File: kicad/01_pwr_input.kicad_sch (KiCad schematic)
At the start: 7 parts, among them J6 2x3 1.27mm (bottom), U101 NCP163ASN330T1G

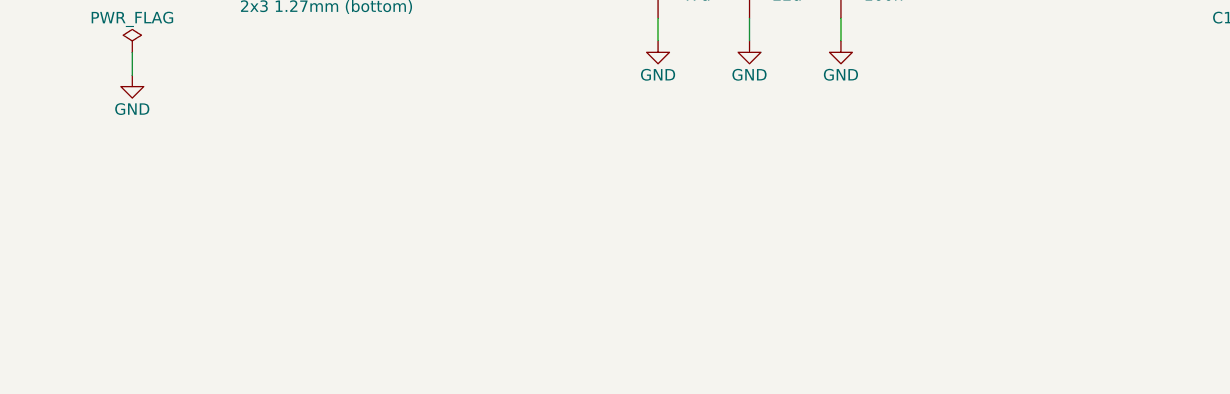
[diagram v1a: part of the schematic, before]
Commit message: J101 bench 5 V header, J3 0.9/0.6 mm pads, baseboard U8 2 A
- J101 (sheet 01): 2.54 mm 1x2 header on F.Cu north-east of J6, pin 1 5V0 / pin 2 GND,
  to power the card with female jumpers without the baseboard. On the 5V0 B.Cu pour and
  the GND planes; nothing on the baseboard under its tails (MECHANICAL.md).
- J3: project-local footprint ti135_card:PinSocket_2x19_P1.27mm_Vertical_Drill0.6
  (pads 0.9 mm, drill 0.6 mm, as on the Agilex card) so a 0.1 mm track fits between pins.
- Baseboard U8 is now the Mornsun K7805-2000R3 (5 V / 2 A; ac_psu_kicad 732c9b1):
  POWER_BUDGET, STATUS and MECHANICAL updated; 20V_ISO_SEC still to be measured.
- Board: also the routing in progress. DRC: schematic parity 0.

Co-Authored-By: Claude Opus 5.5 <noreply@anthropic.com>
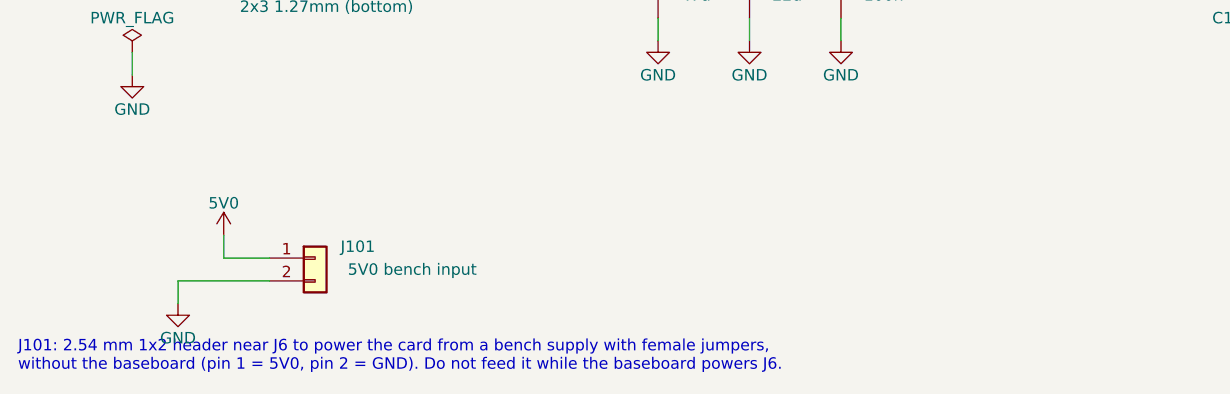
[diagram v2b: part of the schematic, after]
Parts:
- added J101: 5V0 bench input, Connector_PinHeader_2.54mm:PinHeader_1x02_P2.54mm_Vertical, symbol ti135_card:Conn_01x02
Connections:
- net 5V0: now also J101.1 (Pin_1)
- net GND: now also J101.2 (Pin_2)
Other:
- note added: "J101: 2.54 mm 1x2 header near J6 to power the card from a bench supply with female jumpers, without the baseboard (pin 1 = 5V0, pin 2 = GND). Do not feed it while the baseboard powers J6."
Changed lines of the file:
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@@
+		)
+	)
+	(symbol
+		(lib_id "ti135_card:Conn_01x02")
+		(at 50.8 96.52 0)
+		(unit 1)
+		(exclude_from_sim no)
+		(in_bom yes)
+		(on_board yes)
+		(dnp no)
+		(property "Reference" "J101"
+			(at 55.54 95.25 0)
+			(effects
+				(font
+					(size 1.27 1.27)
+				)
+			)
+		)
+		(property "Value" "5V0 bench input"
+			(at 61.59 97.79 0)
+			(effects
+				(font
+					(size 1.27 1.27)
+				)
+			)
+		)
+		(property "Footprint" "Connector_PinHeader_2.54mm:PinHeader_1x02_P2.54mm_Vertical"
+			(at 50.8 96.52 0)
+			(effects
+				(font
+					(size 1.27 1.27)
+				)
+				(hide yes)
+			)
+		)
+		(property "Datasheet" ""
+			(at 50.8 96.52 0)
+			(effects
+				(font
+					(size 1.27 1.27)
+				)
+				(hide yes)
+			)
+		)
+		(property "Description" "Generic connector, single row, 01x02, script generated (kicad-library-utils/schlib/autogen/connector/)"
+			(at 50.8 96.52 0)
+			(effects
+				(font
+					(size 1.27 1.27)
+				)
+				(hide yes)
+			)
+		)
+		(pin "1"
+		)
+		(pin "2"
+		)
+		(instances
+			(project "ti135_card"
+				(path "/c384d3ae-6e7d-47ca-8f4d-7f9f77efe4b7/b177fc93-3c09-44d0-8b93-4373107c4e43"
+					(reference "J101")
+					(unit 1)
+				)
+			)
+		)
+	)
+	(wire
+		(pts
+			(xy 45.72 96.52) (xy 40.64 96.52)
+		)
+		(stroke
+			(width 0)
+			(type default)
+		)
+	)
+	(wire
+		(pts
+			(xy 40.64 96.52) (xy 40.64 93.98)
+		)
+		(stroke
+			(width 0)
+			(type default)
+		)
+	)
+	(symbol
+		(lib_id "ti135_card:5V0")
+		(at 40.64 93.98 0)
+		(unit 1)
+		(exclude_from_sim no)
+		(in_bom yes)
+		(on_board yes)
+		(dnp no)
+		(property "Reference" "#PWR01019"
+			(at 40.64 97.79 0)
+			(effects
+				(font
+					(size 1.27 1.27)
+				)
+				(hide yes)
+			)
+		)
+		(property "Value" "5V0"
+			(at 40.64 90.424 0)
+			(effects
+				(font
+					(size 1.27 1.27)
+				)
+			)
+		)
+		(property "Footprint" ""
+			(at 40.64 93.98 0)
+			(effects
+				(font
+					(size 1.27 1.27)
+				)
+				(hide yes)
+			)
+		)
+		(property "Datasheet" ""
+			(at 40.64 93.98 0)
+			(effects
+				(font
+					(size 1.27 1.27)
+				)
+				(hide yes)
+			)
+		)
+		(property "Description" "Power symbol for net \"5V0\" (IPC net name)"
+			(at 40.64 93.98 0)
+			(effects
+				(font
+					(size 1.27 1.27)
+				)
+				(hide yes)
+			)
+		)
+		(pin "1"
+		)
+		(instances
+			(project "ti135_card"
+				(path "/c384d3ae-6e7d-47ca-8f4d-7f9f77efe4b7/b177fc93-3c09-44d0-8b93-4373107c4e43"
+					(reference "#PWR01019")
+					(unit 1)
+				)
+			)
+		)
+	)
+	(wire
+		(pts
+			(xy 45.72 99.06) (xy 35.56 99.06)
+		)
+		(stroke
+			(width 0)
+			(type default)
+		)
+	)
+	(wire
+		(pts
+			(xy 35.56 99.06) (xy 35.56 101.6)
+		)
+		(stroke
+			(width 0)
+			(type default)
+		)
+	)
+	(symbol
+		(lib_id "ti135_card:GND")
+		(at 35.56 101.6 0)
+		(unit 1)
+		(exclude_from_sim no)
+		(in_bom yes)
+		(on_board yes)
+		(dnp no)
+		(property "Reference" "#PWR01020"
+			(at 35.56 107.95 0)
+			(effects
+				(font
+					(size 1.27 1.27)
+				)
+				(hide yes)
+			)
+		)
+		(property "Value" "GND"
+			(at 35.56 105.41 0)
+			(effects
+				(font
+					(size 1.27 1.27)
+				)
+			)
+		)
+		(property "Footprint" ""
+			(at 35.56 101.6 0)
+			(effects
+				(font
+					(size 1.27 1.27)
+				)
+				(hide yes)
+			)
+		)
+		(property "Datasheet" ""
+			(at 35.56 101.6 0)
+			(effects
+				(font
+					(size 1.27 1.27)
+				)
+				(hide yes)
+			)
+		)
+		(property "Description" "Power symbol for net \"GND\" (IPC net name)"
+			(at 35.56 101.6 0)
+			(effects
+				(font
+					(size 1.27 1.27)
+				)
+				(hide yes)
+			)
+		)
+		(pin "1"
+		)
+		(instances
+			(project "ti135_card"
+				(path "/c384d3ae-6e7d-47ca-8f4d-7f9f77efe4b7/b177fc93-3c09-44d0-8b93-4373107c4e43"
+					(reference "#PWR01020")
+					(unit 1)
+				)
+			)
+		)
+	)
+	(text "J101: 2.54 mm 1x2 header near J6 to power the card from a bench supply with female jumpers,\nwithout the baseboard (pin 1 = 5V0, pin 2 = GND). Do not feed it while the baseboard powers J6."
+		(exclude_from_sim no)
+		(at 17.78 109.22 0)
+		(effects
+			(font
+				(size 1.27 1.27)
+			)
+			(justify left bottom)
 		)
 	)

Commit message: LCSC numbers for all JLC parts; Y701 -> YXC OT322525MJBA4SL
- tools/set_lcsc.py: one table (value, footprint) -> LCSC, fills empty LCSC fields in the
  sheets; 312 symbols. JLC basic parts where available, cap voltages checked per rail,
  VCORE divider 0.1 % (no 0.5 % in stock). Board fields synced with add_parts.py.
- Y701: the SiT8924 has no JLC stock; now YXC OT322525MJBA4SL (C669088, 3225), EN tied
  to 1V8. R701/C701 moved 0.5 mm to clear its courtyard. Netlist change: Y701 pin 1 -> 1V8.
- Only U501 (Ti135) is left without LCSC (global sourcing / consigned).
- DRC: schematic parity 0.

Co-Authored-By: Claude Opus 5.5 <noreply@anthropic.com>
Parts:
- C101: LCSC (none) -> C96123
- C102: LCSC (none) -> C45783
- C103: LCSC (none) -> C1525
- C104, C105: LCSC (none) -> C52923
- J101: LCSC (none) -> C492401
- J6: LCSC (none) -> C22373841
- U101: LCSC (none) -> C603656
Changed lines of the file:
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@@
+			)
+		)
+		(property "LCSC" "C45783"
+			(at 99.06 66.04 0)
+			(effects
+				(font
+					(size 1.27 1.27)
+				)
+				(hide yes)
 			)
 		)
@@
 			)
 		)
+		(property "LCSC" "C22373841"
+			(at 50.8 63.5 0)
+			(effects
+				(font
+					(size 1.27 1.27)
+				)
+				(hide yes)
+			)
+		)
 		(pin "1"
 		)
@@
 			)
 		)
+		(property "LCSC" "C96123"
+			(at 88.9 66.04 0)
+			(effects
+				(font
+					(size 1.27 1.27)
+				)
+				(hide yes)
+			)
+		)
 		(pin "1"
 		)
@@
 			)
 		)
+		(property "LCSC" "C52923"
+			(at 157.48 71.12 0)
+			(effects
+				(font
+					(size 1.27 1.27)
+				)
+				(hide yes)
+			)
+		)
 		(pin "1"
 		)
@@
 			)
 		)
+		(property "LCSC" "C1525"
+			(at 109.22 66.04 0)
+			(effects
+				(font
+					(size 1.27 1.27)
+				)
+				(hide yes)
+			)
+		)
 		(pin "1"
 		)
@@
 			)
 		)
+		(property "LCSC" "C52923"
+			(at 193.04 71.12 0)
+			(effects
+				(font
+					(size 1.27 1.27)
+				)
+				(hide yes)
+			)
+		)
 		(pin "1"
 		)
@@
 			)
 		)
+		(property "LCSC" "C603656"
+			(at 177.8 66.04 0)
+			(effects
+				(font
+					(size 1.27 1.27)
+				)
+				(hide yes)
+			)
+		)
 		(pin "1"
 		)
@@
 			(at 50.8 96.52 0)
 			(effects
+				(font
+					(size 1.27 1.27)
+				)
+				(hide yes)
+			)
+		)
+		(property "LCSC" "C492401"
+			(at 50.8 96.52 0)
+			(effects
